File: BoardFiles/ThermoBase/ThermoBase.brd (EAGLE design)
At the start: 72.3 x 58.9 mm, 22 parts, among them CON1 BARREL_JACK_3PIN, U1 MOSFET_N, U2 MOSFET_N, U3 MOSFET_N, U4 LM317

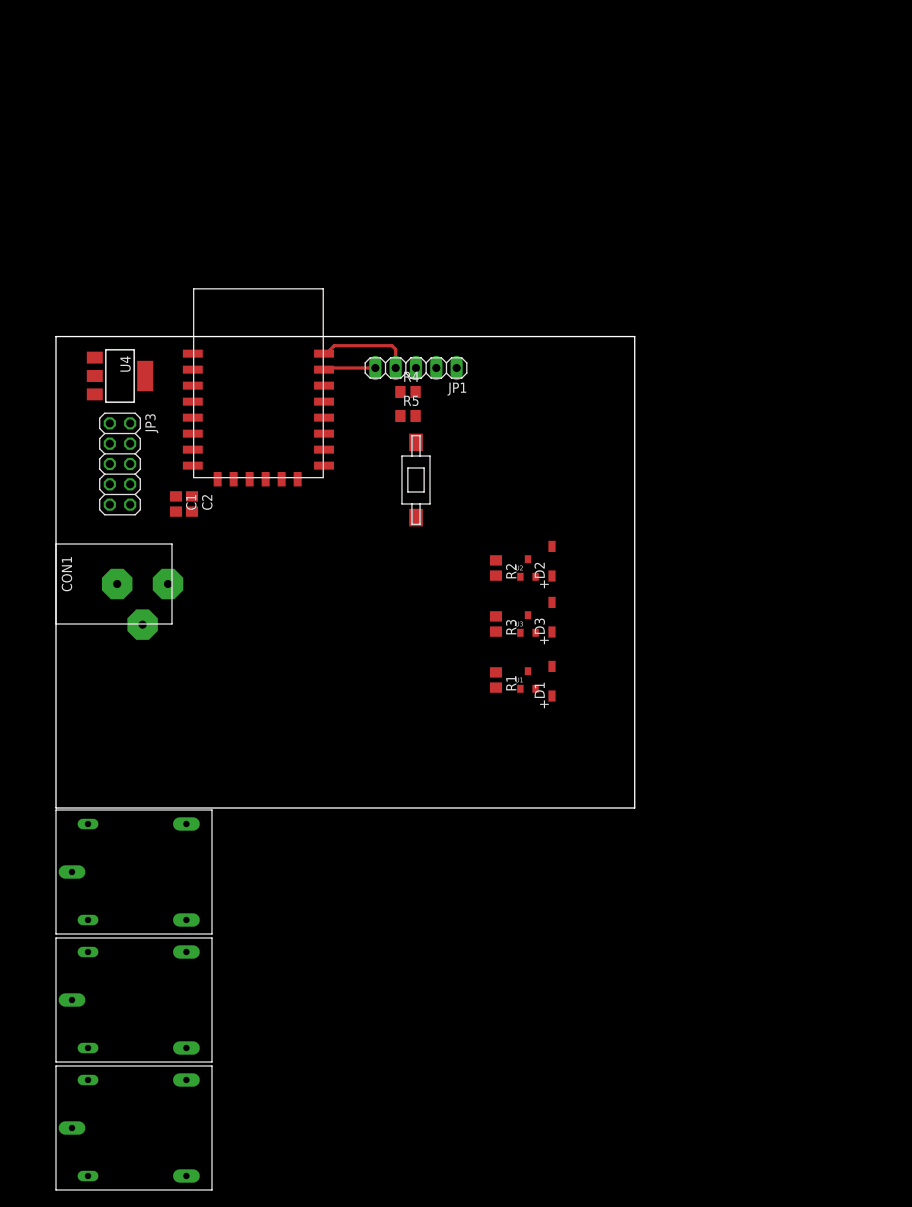
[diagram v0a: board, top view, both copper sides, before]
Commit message: Created LCD Screen holder and updated base board to fit enclosure
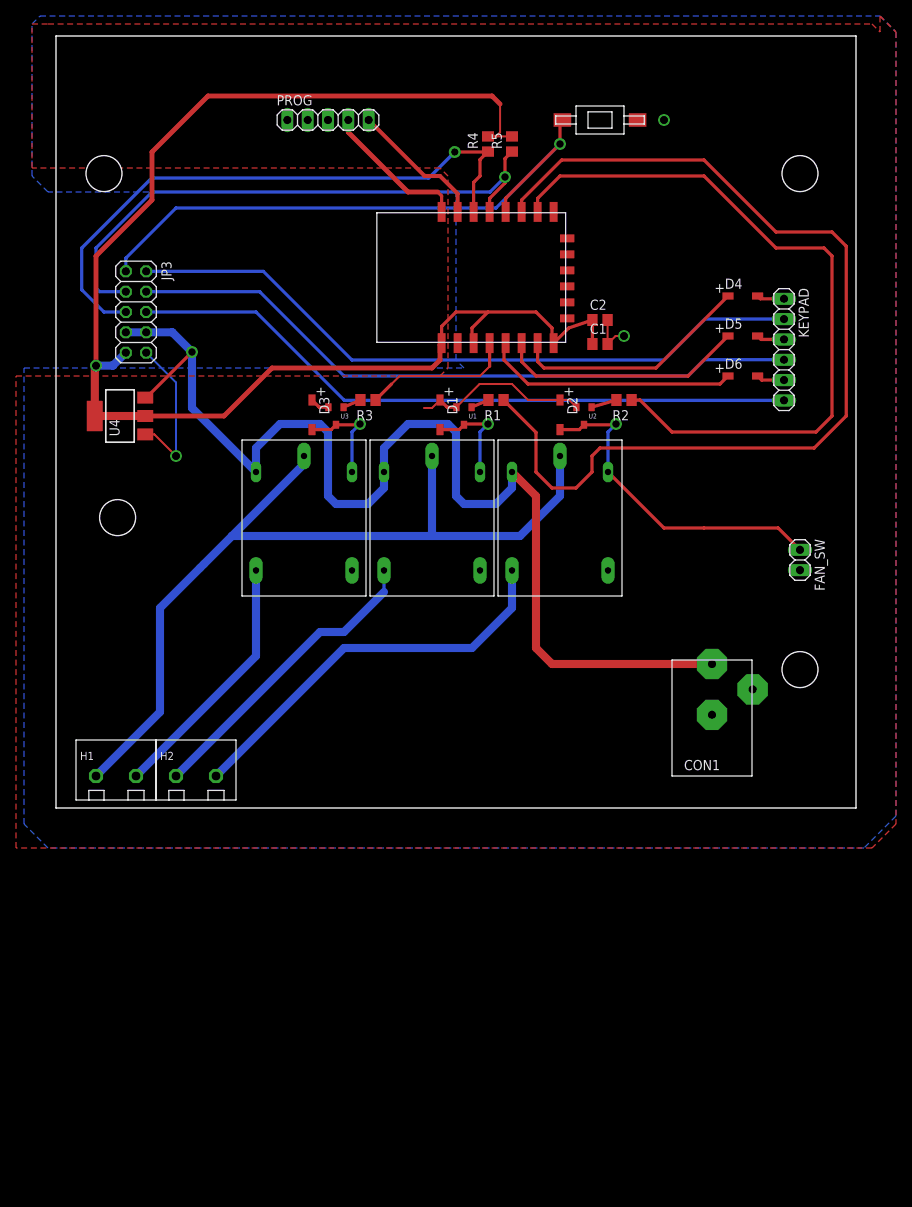
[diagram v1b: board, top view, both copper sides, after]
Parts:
- removed JP1: (no value), pinhead:1X05
- added D4, D5, D6: DIODESOD123, DR:SOD123
- added FAN_SW: (no value), pinhead:1X02
- added H1, H2: TERMBLOCK_5MM_2POS, DR:TERMBLOCK_5MM_2POS
- added KEYPAD: (no value), pinhead:1X06
- added PROG: (no value), pinhead:1X05
- moved RLY3 92.9 mm to (25.0, 44.0), turned to 270 degrees
- moved RLY2 92.2 mm to (57.0, 44.0), turned to 270 degrees
- moved RLY1 69.9 mm to (41.0, 44.0), turned to 270 degrees
- moved CON1 68.7 mm to (82.0, 18.0), turned to 180 degrees
- moved C1 56.6 mm to (68.0, 58.0), turned to 0 degrees
- moved C2 55.9 mm to (68.0, 61.0), turned to 0 degrees
- moved BTN1 50.5 mm to (68.0, 86.0), turned to 0 degrees
- moved U$1 47.6 mm to (62.2, 58.2), turned to 90 degrees
- moved D3 41.7 mm to (32.0, 51.0), turned to 270 degrees
- moved D1 39.6 mm to (48.0, 51.0), turned to 270 degrees
- moved R5 36.4 mm to (57.0, 83.0), turned to 90 degrees
- moved R1 35.0 mm to (55.0, 51.0), turned to 180 degrees
- moved U3 33.9 mm to (35.0, 48.0), turned to 180 degrees
- moved R4 32.6 mm to (54.0, 83.0), turned to 90 degrees
- moved R3 32.2 mm to (39.0, 51.0), turned to 180 degrees
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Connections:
- new net KEY1: JP3.6, KEYPAD.6
- new net KEY2: JP3.4, KEYPAD.4
- new net KEY3: JP3.2, KEYPAD.2
- new net N$12: H1.2, RLY3.4
- new net N$13: D4.2, KEYPAD.1
- new net N$14: D5.2, KEYPAD.3
- new net N$15: D6.2, KEYPAD.5
- new net N$3: H2.1, RLY1.4
- new net N$8: H2.2, RLY2.4
- net GND: now also FAN_SW.2, PROG.1; no longer JP1.1
- net N$1: now also PROG.5; no longer JP1.5
- net N$11: now also H1.1
- net N$2: now also PROG.4; no longer JP1.4
- net N$9: now also FAN_SW.1
- net PB1: now also D6.1, U$1.5; no longer JP3.6, U$1.7
- net PB2: now also D5.1; no longer JP3.4
- net PB3: now also D4.1, U$1.7; no longer JP3.2, U$1.5
- net RLY1: now also U$1.11; no longer U$1.4
- net RLY2: now also U$1.10; no longer U$1.11
- net RLY3: now also U$1.4; no longer U$1.10
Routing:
- net +3V3: track 0.00 -> 176.0 mm, vias 0 -> 1
- net +5V: track 0.00 -> 145.7 mm, vias 0 -> 1
- net RLY1: track 0.00 -> 125.0 mm
- net N$11: track 0.00 -> 108.8 mm
- net RLY2: track 0.00 -> 91.3 mm
- net KEY3: track 0.00 -> 86.4 mm
- net KEY2: track 0.00 -> 84.9 mm
- net KEY1: track 0.00 -> 84.3 mm
- net LCDE: track 0.00 -> 76.4 mm, vias 0 -> 1
- net SDA: track 0.00 -> 75.9 mm, vias 0 -> 1
- net SCL: track 0.00 -> 72.4 mm, vias 0 -> 1
- net N$8: track 0.00 -> 50.4 mm
- net GND: track 0.00 -> 49.6 mm, vias 0 -> 3
- net N$9: track 0.00 -> 41.7 mm, vias 0 -> 1
- net N$3: track 0.00 -> 38.2 mm
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- added copper zone on layer 1, net GND
- added copper zone on layer 16, net GND
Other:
- board size 72.3 x 58.9 mm -> 100 x 96.5 mm

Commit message: Successfully built display board, archived old test software
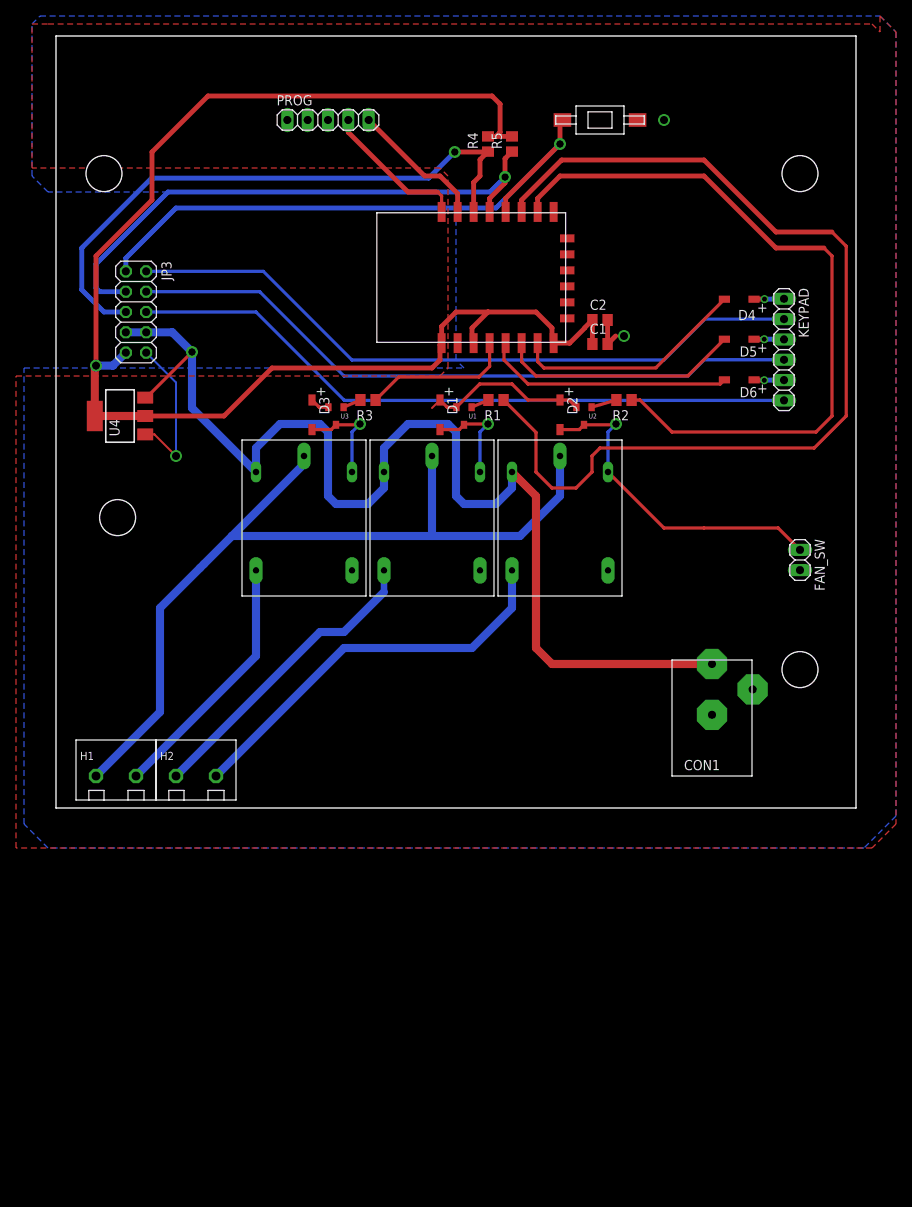
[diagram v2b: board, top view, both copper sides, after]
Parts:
- moved D6 3.29 mm to (87.3, 53.5), turned to 180 degrees
- moved D4 3.27 mm to (87.2, 63.6), turned to 180 degrees
- moved D5 3.27 mm to (87.2, 58.6), turned to 180 degrees
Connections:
- net N$13: now also D4.1; no longer D4.2
- net N$14: now also D5.1; no longer D5.2
- net N$15: now also D6.1; no longer D6.2
- net PB1: now also D6.2; no longer D6.1
- net PB2: now also D5.2; no longer D5.1
- net PB3: now also D4.2; no longer D4.1
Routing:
- net SCL: track 72.4 -> 71.3 mm
- net GND: track 49.6 -> 48.6 mm
- net PB1: track 31.8 -> 31.2 mm
- net PB3: track 30.2 -> 29.6 mm
- net PB2: track 30.9 -> 30.3 mm
- net N$13: track 3.44 -> 3.77 mm, vias 0 -> 1
- net N$14: track 3.48 -> 3.79 mm, vias 0 -> 1
- net N$15: track 3.51 -> 3.78 mm, vias 0 -> 1

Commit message: Few Tweaks
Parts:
- moved CON1 1.00 mm to (81.0, 18.0)
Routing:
- net +5V: track 145.7 -> 144.7 mm
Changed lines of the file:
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@@
 <wire x1="100" y1="96.5" x2="0" y2="96.5" width="0" layer="20"/>
 <wire x1="0" y1="96.5" x2="0" y2="0" width="0" layer="20"/>
-<hole x="93" y="17.3" drill="4.5"/>
-<hole x="93" y="79.3" drill="4.5"/>
+<hole x="93.5" y="17.3" drill="4.5"/>
+<hole x="93.5" y="79.3" drill="4.5"/>
 <hole x="7.7" y="36.3" drill="4.5"/>
 <hole x="6" y="79.3" drill="4.5"/>
@@
 </element>
 <element name="BTN1" library="DR" package="SMD-2-SWITCH" value="FSMSM_SWITCH_6X3.6" x="68" y="86" smashed="yes"/>
-<element name="CON1" library="DR" package="PJ-102A" value="BARREL_JACK_3PIN" x="82" y="18" smashed="yes" rot="R180">
-<attribute name="NAME" x="83" y="6" size="1.27" layer="21" rot="R180"/>
+<element name="CON1" library="DR" package="PJ-102A" value="BARREL_JACK_3PIN" x="81" y="18" smashed="yes" rot="R180">
+<attribute name="NAME" x="81" y="6" size="1.27" layer="21" rot="R180"/>
 </element>
 <element name="C1" library="DR" package="C0805" value="" x="68" y="58" smashed="yes">
@@
 <wire x1="57" y1="42" x2="60" y2="39" width="1.016" layer="1"/>
 <wire x1="60" y1="20" x2="62" y2="18" width="1.016" layer="1"/>
-<wire x1="62" y1="18" x2="82" y2="18" width="1.016" layer="1"/>
+<wire x1="62" y1="18" x2="81" y2="18" width="1.016" layer="1"/>
 <wire x1="60" y1="39" x2="60" y2="20" width="1.016" layer="1"/>
 <wire x1="25" y1="42" x2="17" y2="50" width="1.016" layer="16"/>

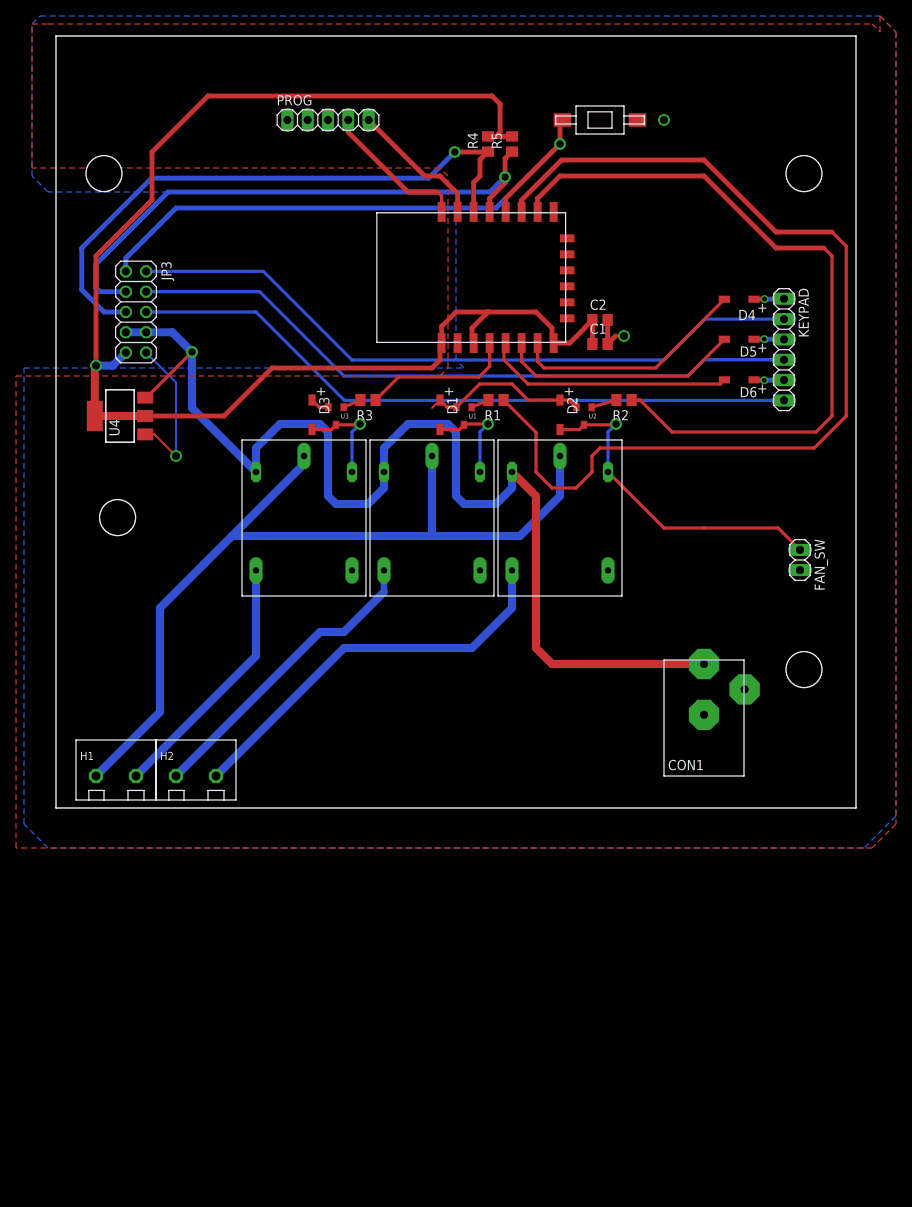
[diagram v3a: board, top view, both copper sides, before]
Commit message: Changes for keypad
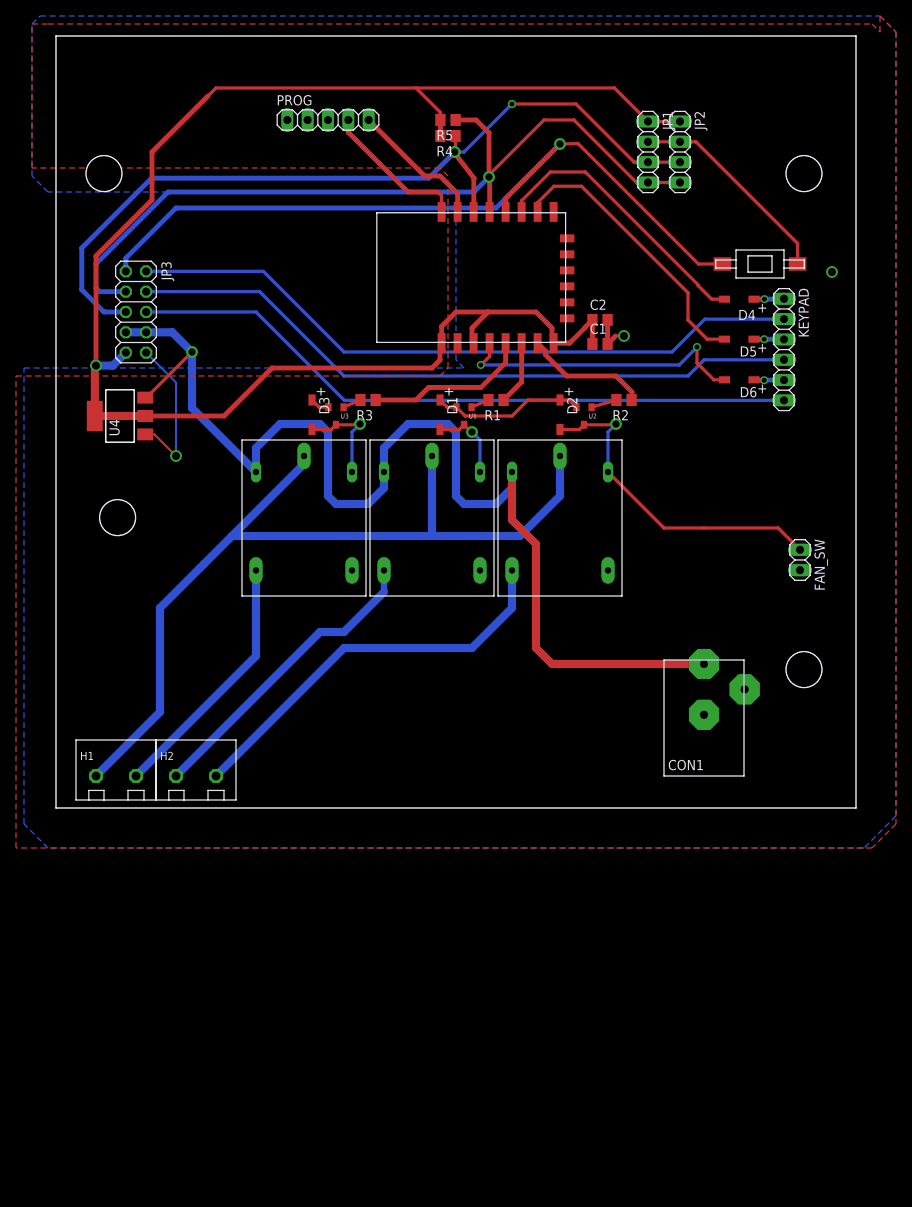
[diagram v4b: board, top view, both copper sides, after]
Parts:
- added JP1, JP2: (no value), pinhead:1X04
- moved BTN1 26.9 mm to (88.0, 68.0)
- moved R5 8.54 mm to (49.0, 86.0), turned to 180 degrees
- moved R4 5.10 mm to (49.0, 84.0), turned to 180 degrees
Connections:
- net +3V3: now also JP1.1, JP2.1
- net GND: now also JP1.2, JP2.2
- net PB1: now also U$1.4; no longer U$1.5
- net PB2: now also U$1.10; no longer U$1.6
- net PB3: now also U$1.11; no longer U$1.7
- net RLY1: now also U$1.6; no longer U$1.11
- net RLY2: now also U$1.7; no longer U$1.10
- net RLY3: now also U$1.5; no longer U$1.4
- net SCL: now also JP1.4, JP2.4
- net SDA: now also JP1.3, JP2.3
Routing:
- net RLY1: track 125.0 -> 8.04 mm
- net RLY2: track 91.3 -> 15.6 mm
- net SCL: track 71.3 -> 105.7 mm
- net SDA: track 75.9 -> 107.5 mm, vias 1 -> 2
- net GND: track 48.6 -> 72.9 mm
- net +3V3: track 176.3 -> 200.5 mm
- net LCDE: track 76.4 -> 99.7 mm
- net PB1: track 31.2 -> 37.5 mm, vias 0 -> 2
- net PB3: track 29.6 -> 34.9 mm
- net PB2: track 30.3 -> 35.3 mm
- net N$7: track 12.7 -> 10.0 mm
- net RLY3: track 18.9 -> 20.6 mm
- net KEY3: track 86.4 -> 85.6 mm

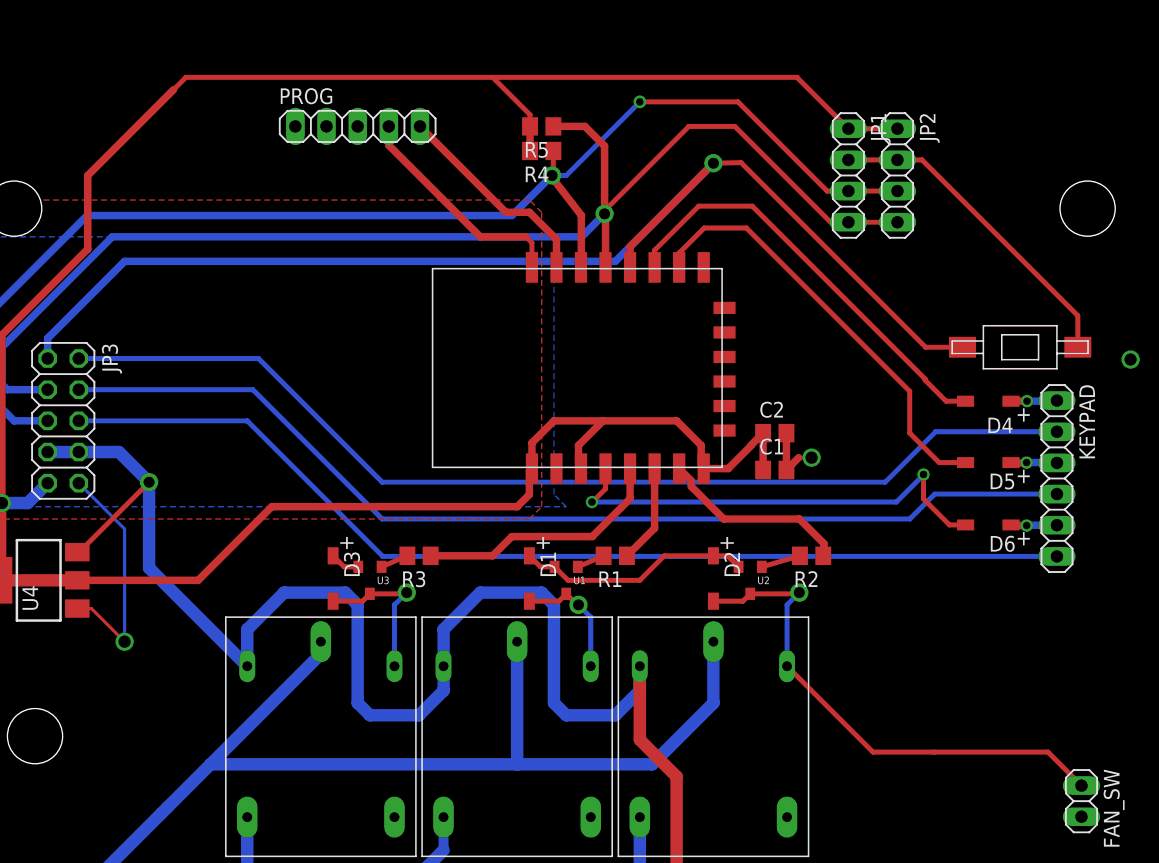
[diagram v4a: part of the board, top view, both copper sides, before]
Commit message: Tweaked some small leads to be bigger
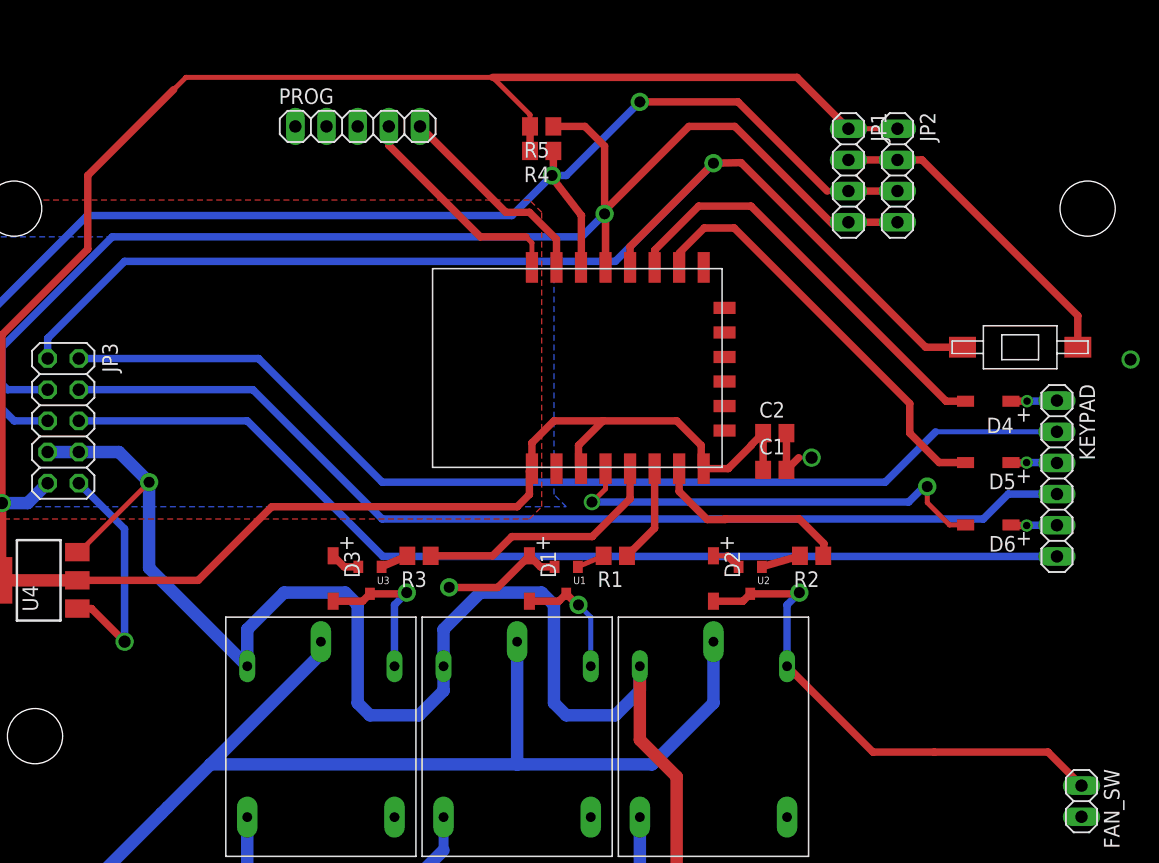
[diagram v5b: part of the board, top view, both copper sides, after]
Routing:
- net GND: track 72.9 -> 66.2 mm, vias 3 -> 4
- net PB1: track 37.5 -> 36.3 mm
- net RLY2: track 15.6 -> 16.7 mm
- net PB2: track 35.3 -> 34.7 mm
